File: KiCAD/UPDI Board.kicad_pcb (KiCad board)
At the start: 2 copper layers, 19.1 x 30.5 mm, 21 parts, among them J1 AVR UPDI Header, J10 Primary Header, J12 Second Header, J13 RS485, J14 UART0, J15 UPDI, J16 Voltage in, J17 UART1, U7 MAX3072E

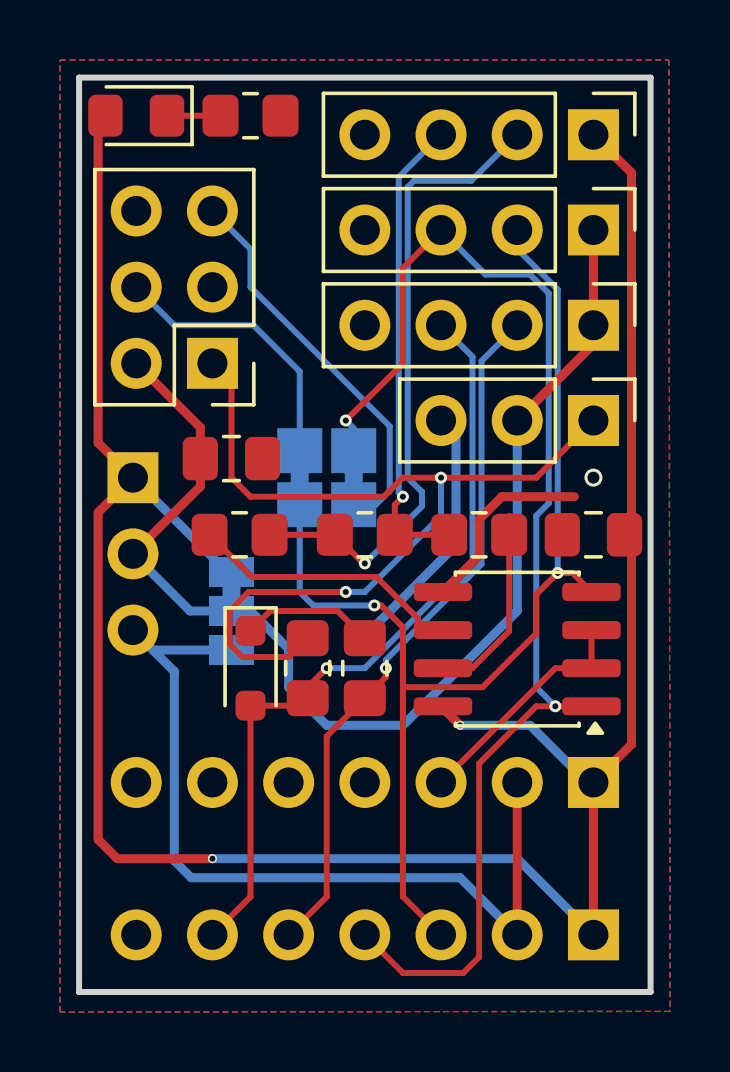
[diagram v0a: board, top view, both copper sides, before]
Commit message: Clean up and add LED
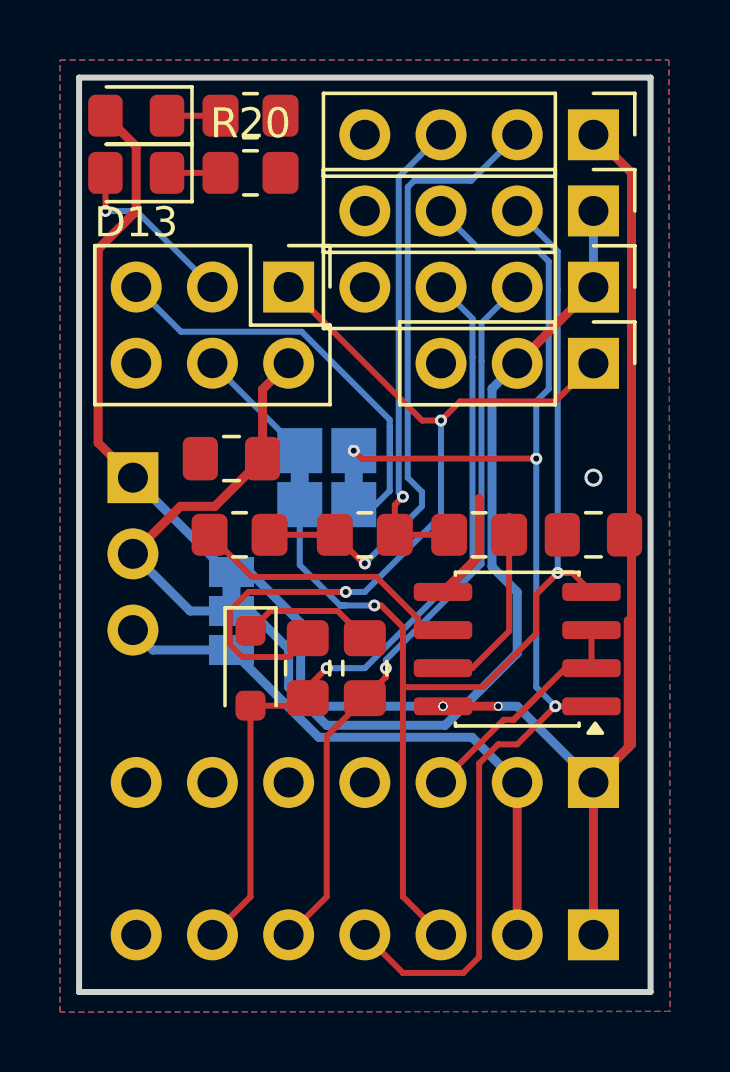
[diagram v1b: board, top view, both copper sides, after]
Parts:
- added D13: Feedback LED, LED_SMD:LED_0805_2012Metric_Pad1.15x1.40mm_HandSolder, F.Cu at (167.0, 43.8)
- added R20: 470, Resistor_SMD:R_0805_2012Metric_Pad1.20x1.40mm_HandSolder, F.Cu at (170.8, 43.8)
- moved J1 3.60 mm to (172.1, 47.6), turned to -90 degrees
- moved J15 1.91 mm to (182.2, 50.2)
- moved J17 1.27 mm to (182.2, 47.6)
- moved J14 0.63 mm to (182.2, 45.1)
- turned C18 to 180 degrees
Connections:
- J1 pad 3: unconnected-(J1-Pin_3-Pad3) -> Net-(D13-A)
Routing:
- net +5V: track 80.2 -> 67.2 mm, vias 2 -> 3
- net GND: track 14.8 -> 3.85 mm
- net +3V3: track 29.4 -> 20.0 mm
- net Net-(D13-A): track 0.00 -> 5.89 mm, vias 0 -> 1
- net /TX0_poka: track 9.25 -> 4.12 mm
- net +Ve: track 38.3 -> 42.1 mm
- net /RX0_poka: track 13.2 -> 15.1 mm
- net Net-(D13-K): track 0.00 -> 1.78 mm
- net /RX0: track 43.0 -> 41.3 mm, vias 2 -> 3
- net /RTS0: track 7.86 -> 9.16 mm
- net /TX1: track 23.1 -> 24.4 mm
- net /RX1: track 25.3 -> 26.6 mm
- net /TX0: track 37.9 -> 38.8 mm
